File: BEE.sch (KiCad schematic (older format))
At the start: 72 parts, among them J1 RPI1_header, J10 Conn_01x02, J11 Conn_01x02, J12 Conn_01x02, J13 Conn_01x06, J14 Conn_01x03, J15 Conn_01x10, J16 Conn_01x08, J17 Conn_01x03, J18 Conn_01x03, J19 Conn_01x03, J2 Conn_02x05_Odd_Even, J3 Conn_01x03, J4 Conn_01x06, J5 Conn_02x10_Odd_Even, J6 Conn_01x06, J7 Conn_02x10_Odd_Even, J8 Conn_01x08, J9 Conn_01x02, SW1 SW_Push, SW2 SW_Push, SW3 SW_Push, U1 MCP3008, U2 MCP4911, U3 Dip_10xsp3t, U4 Dip_10xsp3t, U5 74HC595, U6 Display_7Segments

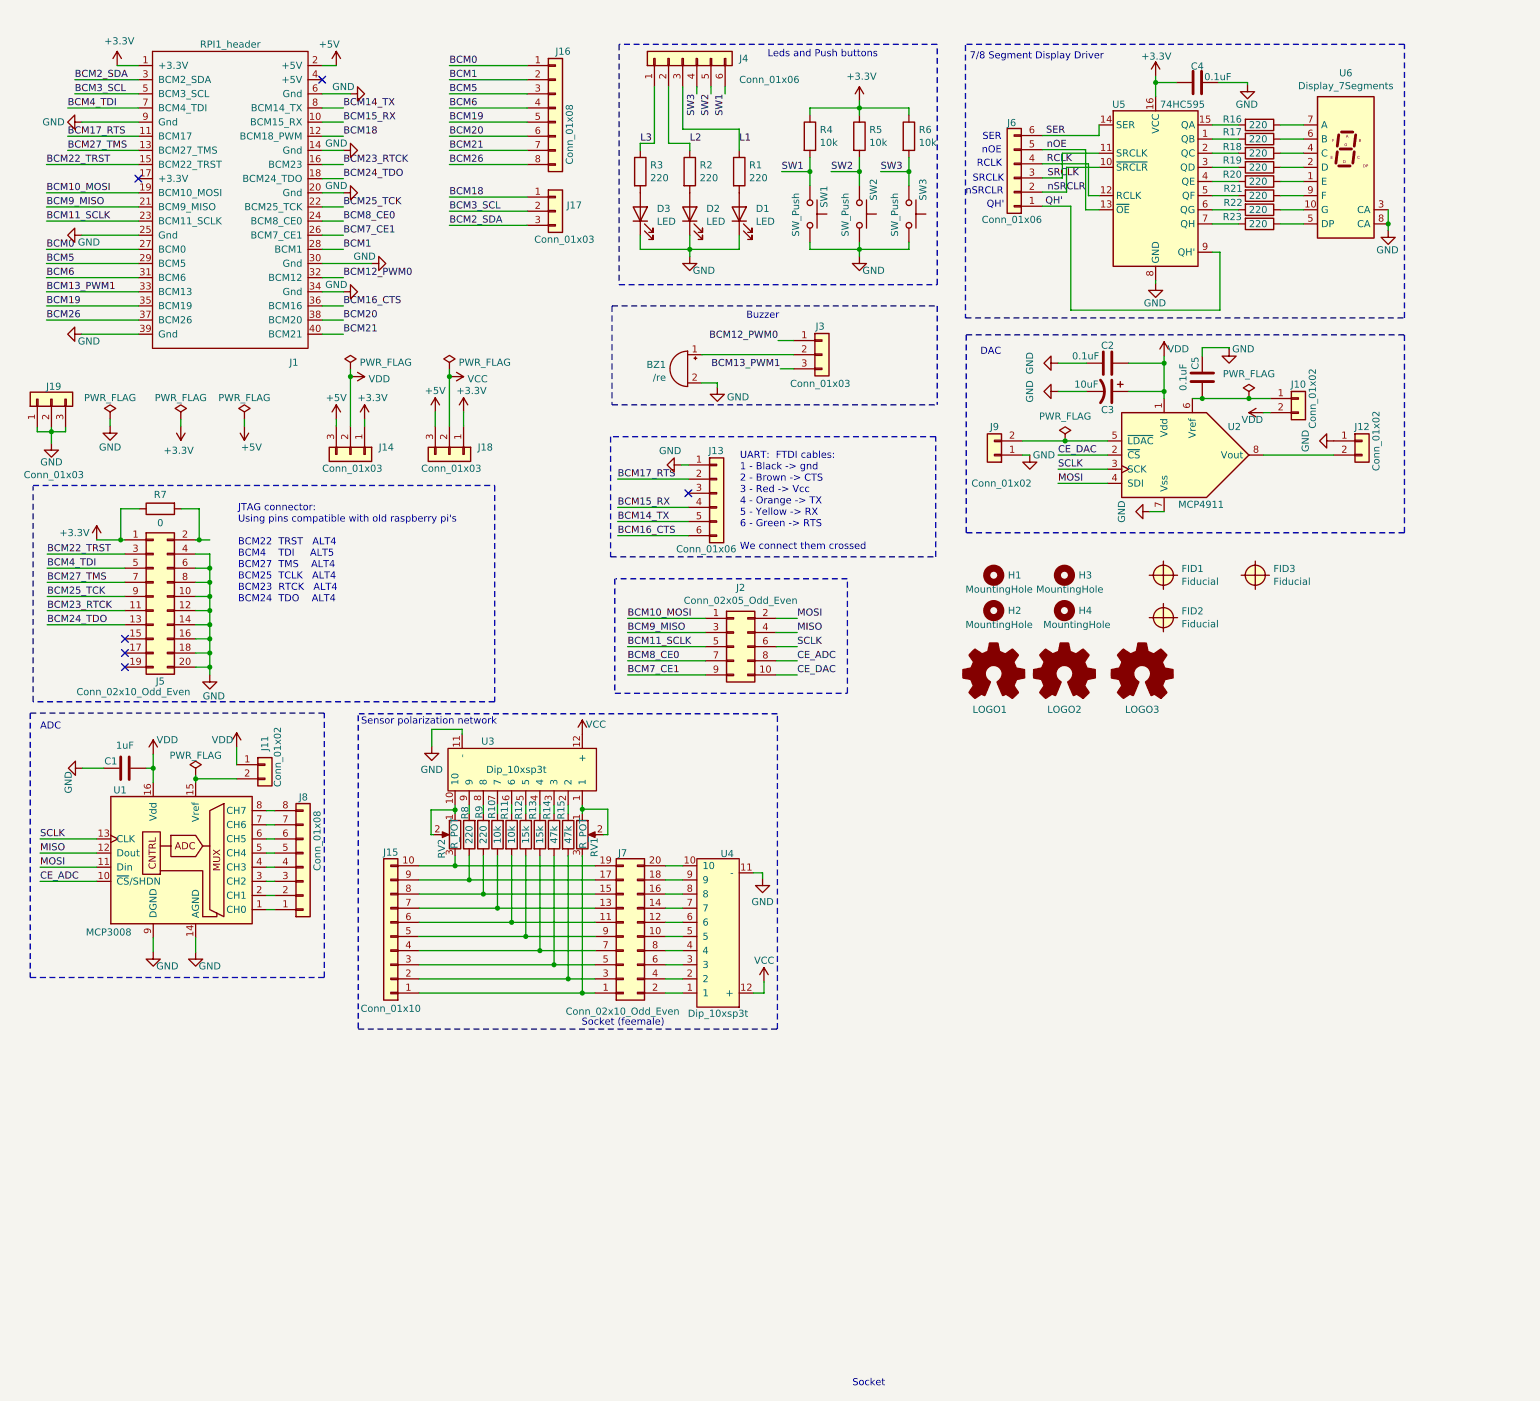
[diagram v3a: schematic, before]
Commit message: Extra pin headers in polarization network and 3d models
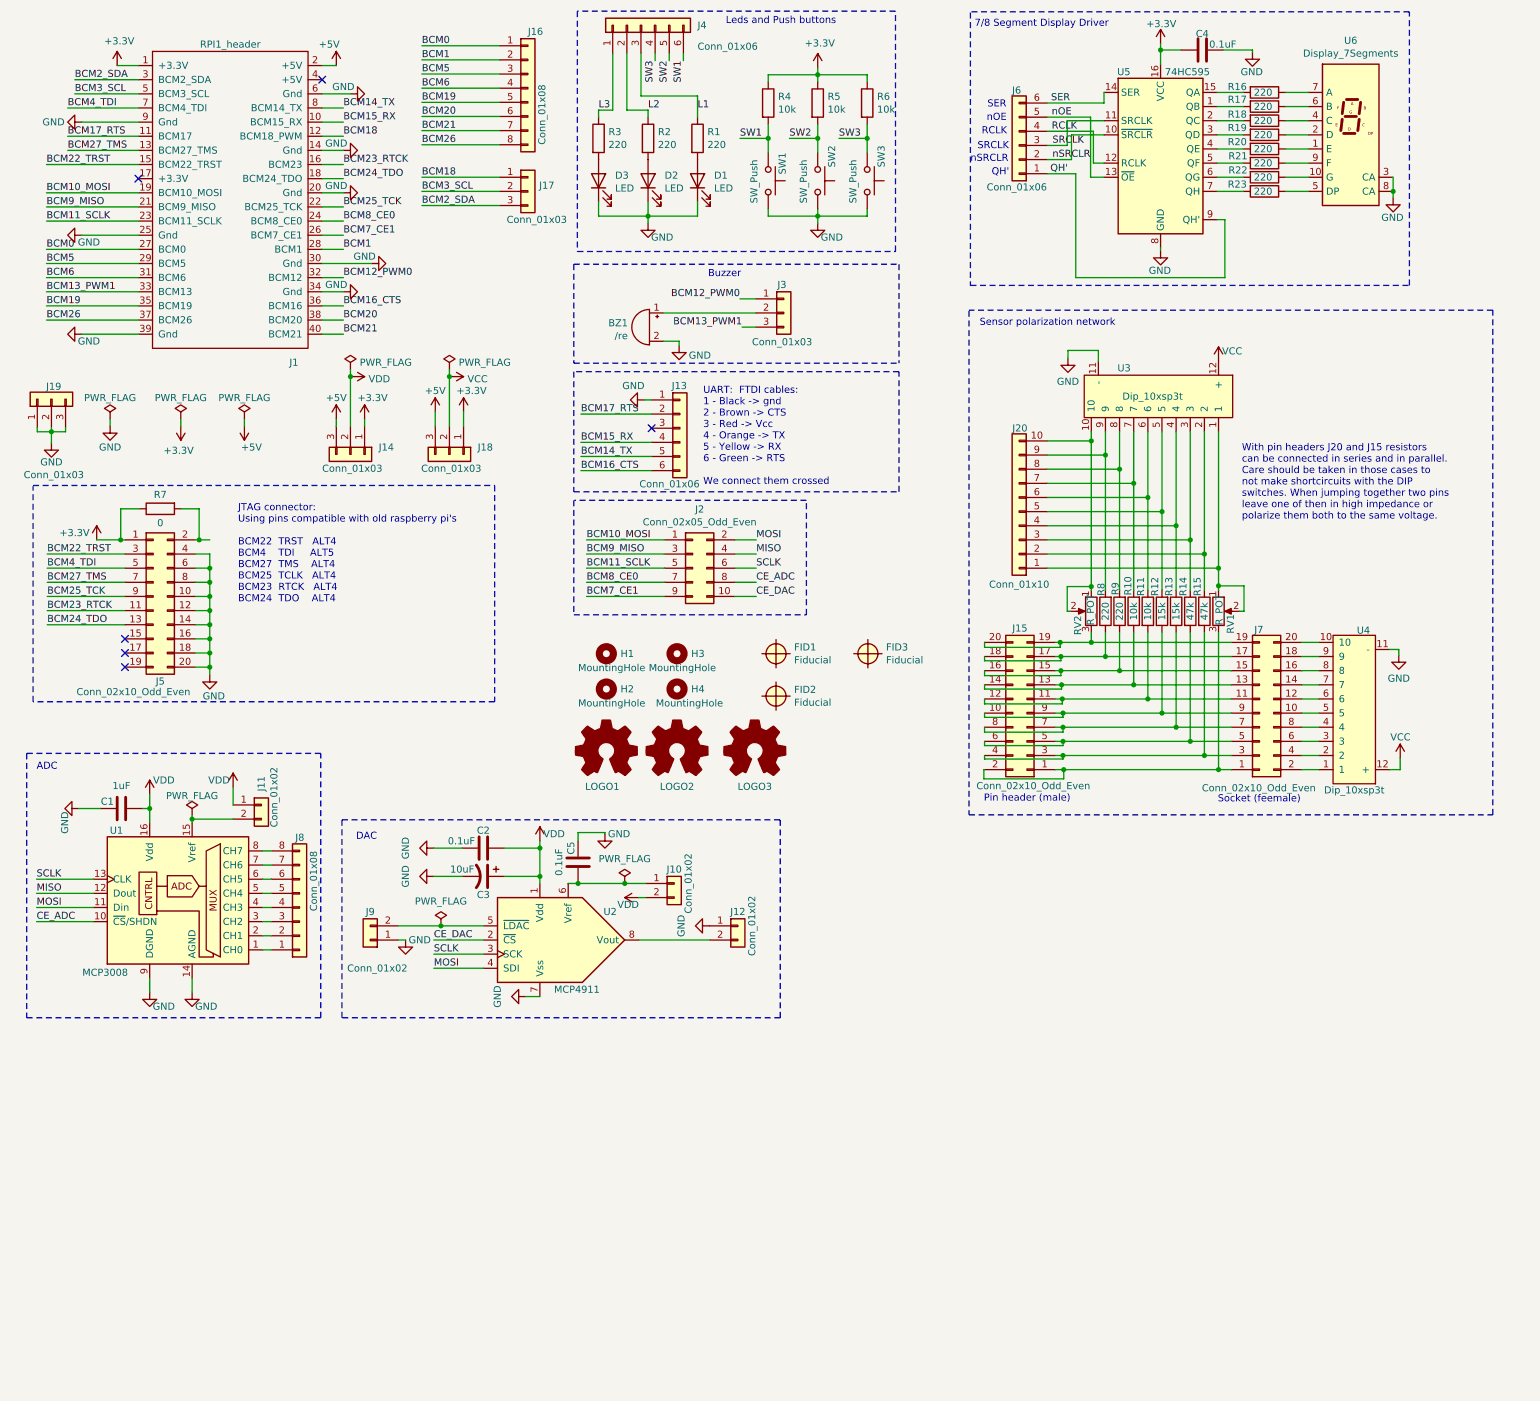
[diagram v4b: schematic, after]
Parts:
- removed J15: Conn_01x10, Connector_PinHeader_2.54mm:PinHeader_1x10_P2.54mm_Vertical, symbol Connector_Generic:Conn_01x10
- added J15: Conn_02x10_Odd_Even, Connector_PinHeader_2.54mm:PinHeader_2x10_P2.54mm_Vertical, symbol Connector_Generic:Conn_02x10_Odd_Even
- added J20: Conn_01x10, Connector_PinHeader_2.54mm:PinHeader_1x10_P2.54mm_Vertical, symbol Connector_Generic:Conn_01x10
- J7: Distributor (none) -> Mouser; Distributor PN (none) -> 710-61301021821; Distributor link (none) -> https://www.mouser.es/ProductDetail/Wurth-Elektronik/613010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; Manufacturer (none) -> Wurth Elektronik; Manufacturer PN (none) -> 61301021821
- SW1, SW2, SW3: footprint BEElib:Push Button -> BEElib:PushButton
- U1: Distributor (none) -> Mouser; Distributor PN (none) -> 579-MCP3008T-I/SL; Distributor link (none) -> https://www.mouser.es/ProductDetail/Microchip-Technology/MC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; Manufacturer (none) -> Microchip Technologies; Manufacturer PN (none) -> MCP3008T-I/SL
- U2: Manufacturer PN MCP4911-E/SN -> CP3008T-I/SL
- U3, U4: Distributor (none) -> Mouser; Distributor PN (none) -> 506-TDS10SGRNTU04; Distributor link (none) -> https://www.mouser.es/ProductDetail/TE-Connectivity-Alcoswi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; Manufacturer (none) -> TE Connectivity / Alcoswitch; Manufacturer PN (none) -> TDS10SGRNTU04
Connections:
- net at J7.15 (Pin_15), R9.1: now also J15.15 (Pin_15), J15.16 (Pin_16)
- net at R9.2, U3.8: now also J20.8 (Pin_8)
- net at R11.1, U3.6: now also J20.6 (Pin_6)
- net at J7.11 (Pin_11), R11.2: now also J15.11 (Pin_11), J15.12 (Pin_12)
- net at J7.9 (Pin_9), R12.1: now also J15.10 (Pin_10), J15.9 (Pin_9)
- net at R12.2, U3.5: now also J20.5 (Pin_5)
- net at R15.1, U3.2: now also J20.2 (Pin_2)
- net at J7.3 (Pin_3), R15.2: now also J15.3 (Pin_3), J15.4 (Pin_4)
- net at R14.1, U3.3: now also J20.3 (Pin_3)
- net at J7.5 (Pin_5), R14.2: now also J15.5 (Pin_5), J15.6 (Pin_6)
- net at R13.1, U3.4: now also J20.4 (Pin_4)
- net at J7.7 (Pin_7), R13.2: now also J15.7 (Pin_7), J15.8 (Pin_8)
- net at J7.13 (Pin_13), R10.1: now also J15.13 (Pin_13), J15.14 (Pin_14)
- net at R10.2, U3.7: now also J20.7 (Pin_7)
- net at J7.17 (Pin_17), R8.1: now also J15.17 (Pin_17), J15.18 (Pin_18)
- net at R8.2, U3.9: now also J20.9 (Pin_9)
- net at RV1.1, RV1.2, U3.1: now also J20.1 (Pin_1)
- net at J7.1 (Pin_1), RV1.3: now also J15.1 (Pin_1), J15.2 (Pin_2)
- net at RV2.1, RV2.2, U3.10: now also J20.10 (Pin_10)
- net at J7.19 (Pin_19), RV2.3: now also J15.19 (Pin_19), J15.20 (Pin_20)
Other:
- note added: "Pin header (male)"
- note added: "With pin headers J20 and J15 resistors\ncan be connected in series and in parallel.\nCare should be taken in those cases to \nnot make shortcircuits with the DIP \nswitches. When jumping together two pins\nleave one of then in high impedance or\npolarize them both to the same voltage."
- note removed: "Socket"
- moved on the sheet: BZ1, C1, C2, C3, C4, C5, D1, D2, D3, FID1, FID2, FID3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

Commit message: Bit endianness change in display shifter, and some other minor changes to that driver
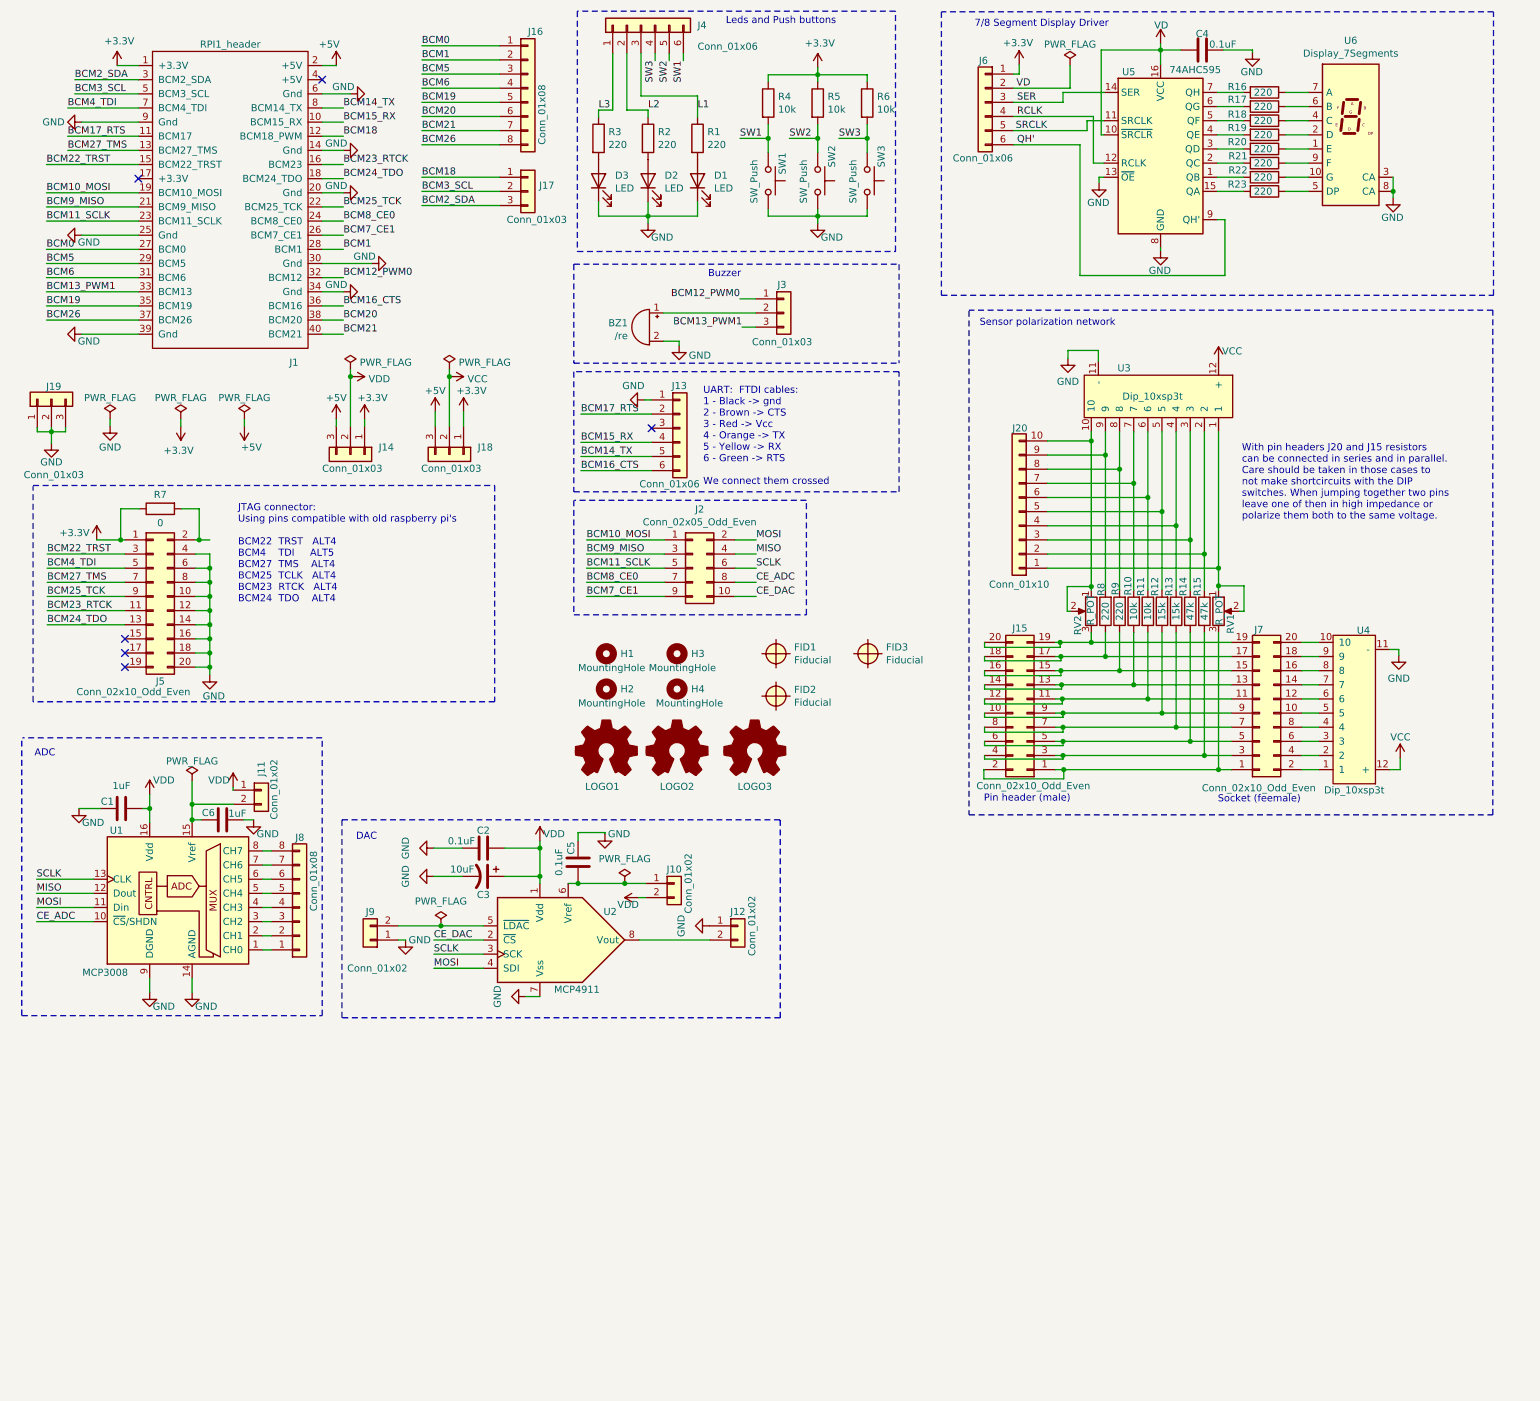
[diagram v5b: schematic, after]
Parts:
- removed U5: 74HC595, Package_SO:SOIC-16_3.9x9.9mm_P1.27mm, symbol 74xx:74HC595
- added C6: 1uF, Capacitor_SMD:C_0805_2012Metric_Pad1.18x1.45mm_HandSolder, symbol Device:C
- added U5: 74AHC595, Package_SO:SOIC-16_3.9x9.9mm_P1.27mm, symbol BEE:74AHC595
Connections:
- net nOE is gone; now on net SRCLK: J6.5 (Pin_5)
- net +3V3: now also J6.1 (Pin_1); no longer C4.1
- net GND: now also C6.1, U5.13 (~OE), U5.8 (GND)
- net QH': now also J6.6 (Pin_6), U5.9 (QH'); no longer J6.1 (Pin_1)
- net RCLK: now also U5.12 (RCLK)
- net SER: now also J6.3 (Pin_3), U5.14 (SER); no longer J6.6 (Pin_6)
- net SRCLK: now also U5.11 (SRCLK); no longer J6.3 (Pin_3)
- net at J11.2 (Pin_2), U1.15 (Vref): now also C6.2
- net at R17.2: now also U5.6 (QG)
- net at R16.2: now also U5.7 (QH)
- net at R18.2: now also U5.5 (QF)
- net at R19.2: now also U5.4 (QE)
- net at R20.2: now also U5.3 (QD)
- net at R21.2: now also U5.2 (QC)
- net at R22.2: now also U5.1 (QB)
- net at R23.2: now also U5.15 (QA)
- net nSRCLR renamed VD
- net VD: now also C4.1, U5.10 (~SRCLR), U5.16 (VCC)
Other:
- note removed: "QH'"
- note removed: "RCLK"
- note removed: "SER"
- note removed: "SRCLK"
- note removed: "nOE"
- note removed: "nSRCLR\n"
- moved on the sheet: J11
